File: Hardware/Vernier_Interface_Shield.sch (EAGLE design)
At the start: 43 parts, among them U1 74HC4052SO, U2 LMV358SOICT

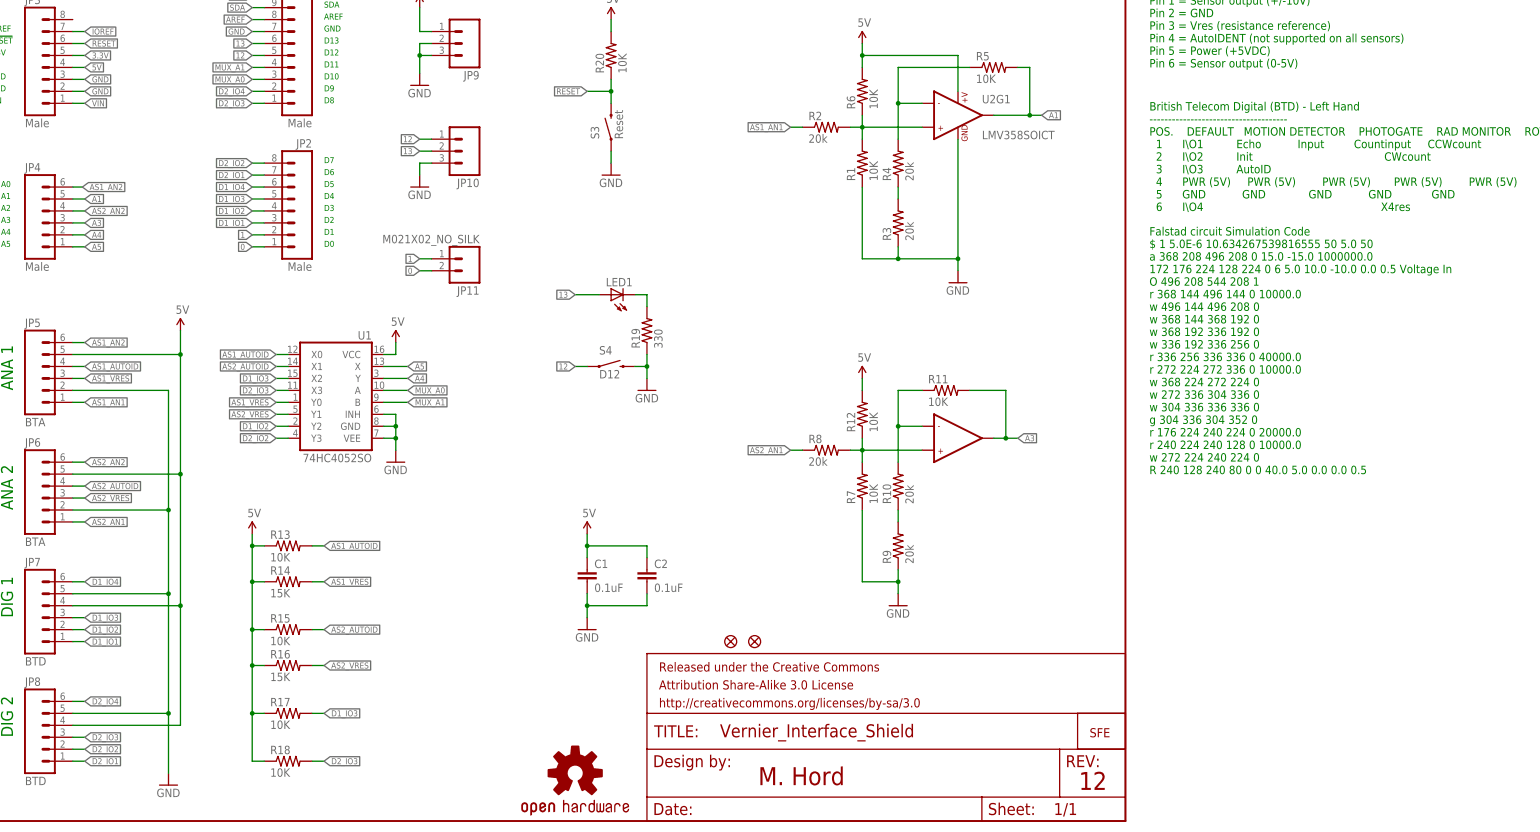
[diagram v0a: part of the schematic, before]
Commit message: Changed silk to fix bug #4
Changed silk to start at IO0 instead of IO1. This is per Vernier's
request.
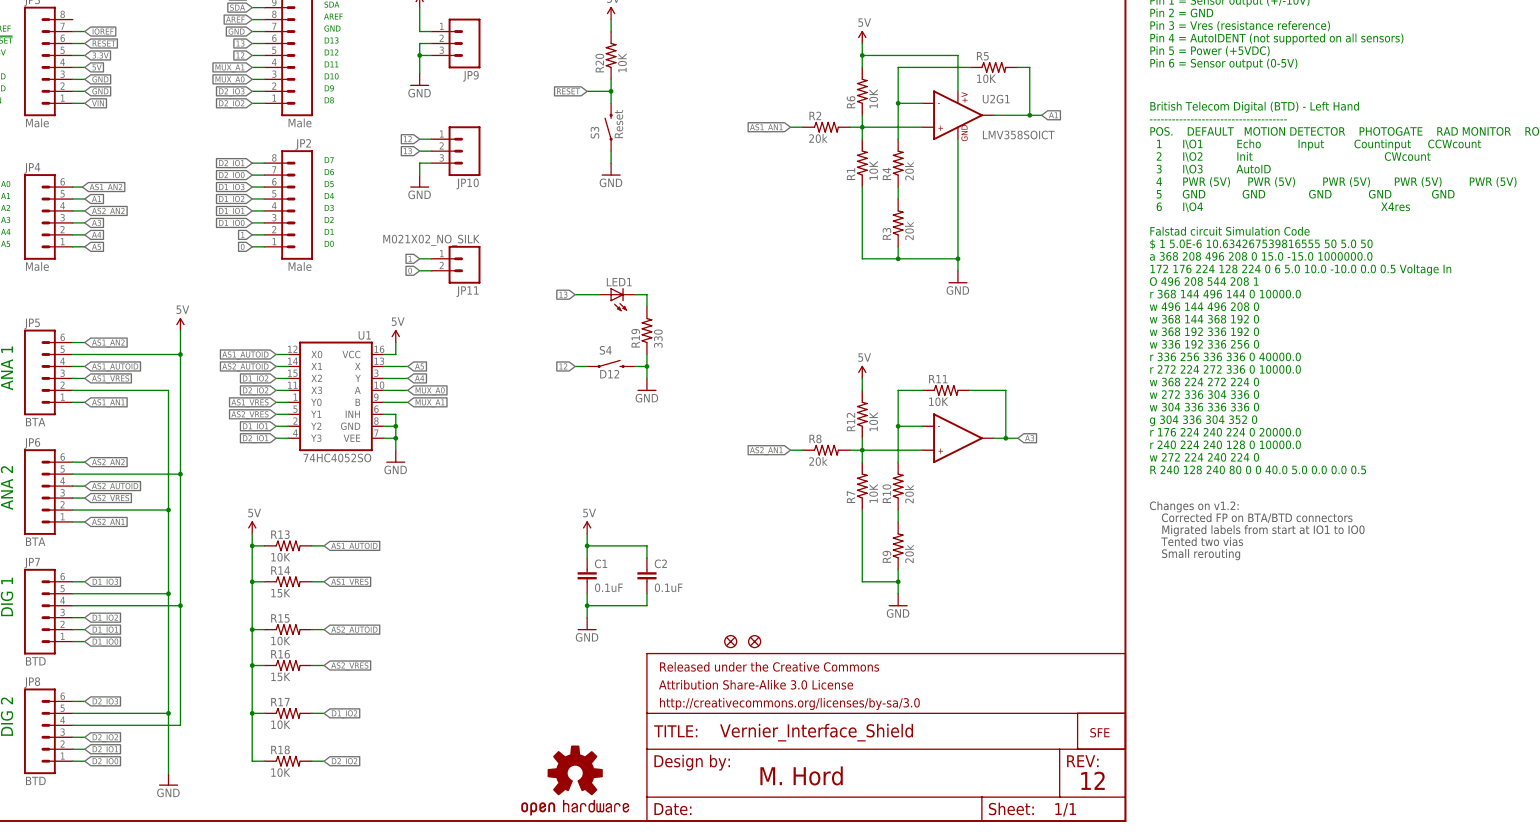
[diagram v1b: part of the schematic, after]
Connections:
- removed net D1_IO4: JP2.6, JP7.6
- removed net D2_IO4: JP1.2, JP8.6
- new net D1_IO0: JP2.3, JP7.1
- new net D2_IO0: JP2.7, JP8.1
- net D1_IO1: now also JP2.4, JP7.2, U1.Y2; no longer JP2.3, JP7.1
- net D1_IO2: now also JP2.5, JP7.3, R17.2, U1.X2; no longer JP2.4, JP7.2, U1.Y2
- net D1_IO3: now also JP2.6, JP7.6; no longer JP2.5, JP7.3, R17.2, U1.X2
- net D2_IO1: now also JP2.8, JP8.2, U1.Y3; no longer JP2.7, JP8.1
- net D2_IO2: now also JP1.1, JP8.3, R18.2, U1.X3; no longer JP2.8, JP8.2, U1.Y3
- net D2_IO3: now also JP1.2, JP8.6; no longer JP1.1, JP8.3, R18.2, U1.X3
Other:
- note added: "Changes on v1.2:"
- note added: "Corrected FP on BTA/BTD connectors"
- note added: "Migrated labels from start at IO1 to IO0"
- note added: "Small rerouting"
- note added: "Tented two vias"
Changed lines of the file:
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@@
 w 272 224 240 224 0
 R 240 128 240 80 0 0 40.0 5.0 0.0 0.0 0.5</text>
+<text x="254" y="66.04" size="1.778" layer="97">Changes on v1.2:</text>
+<text x="256.54" y="63.5" size="1.778" layer="97">Corrected FP on BTA/BTD connectors</text>
+<text x="256.54" y="60.96" size="1.778" layer="97">Migrated labels from start at IO1 to IO0</text>
+<text x="256.54" y="58.42" size="1.778" layer="97">Tented two vias</text>
+<text x="256.54" y="55.88" size="1.778" layer="97">Small rerouting</text>
 </plain>
 <instances>
@@
 </segment>
 </net>
-<net name="D2_IO4" class="0">
+<net name="D2_IO3" class="0">
 <segment>
 <wire x1="25.4" y1="25.4" x2="27.94" y2="25.4" width="0.1524" layer="91"/>
@@
 </segment>
 </net>
-<net name="D2_IO3" class="0">
+<net name="D2_IO2" class="0">
 <segment>
 <wire x1="25.4" y1="17.78" x2="27.94" y2="17.78" width="0.1524" layer="91"/>
@@
 </segment>
 </net>
-<net name="D2_IO2" class="0">
+<net name="D2_IO1" class="0">
 <segment>
 <wire x1="25.4" y1="15.24" x2="27.94" y2="15.24" width="0.1524" layer="91"/>
@@
 </segment>
 </net>
-<net name="D2_IO1" class="0">
+<net name="D2_IO0" class="0">
 <segment>
 <wire x1="25.4" y1="12.7" x2="27.94" y2="12.7" width="0.1524" layer="91"/>
@@
 </segment>
 </net>
-<net name="D1_IO4" class="0">
+<net name="D1_IO3" class="0">
 <segment>
 <wire x1="25.4" y1="50.8" x2="27.94" y2="50.8" width="0.1524" layer="91"/>
@@
 </segment>
 </net>
-<net name="D1_IO3" class="0">
+<net name="D1_IO2" class="0">
 <segment>
 <wire x1="25.4" y1="43.18" x2="27.94" y2="43.18" width="0.1524" layer="91"/>
@@
 </segment>
 </net>
-<net name="D1_IO2" class="0">
+<net name="D1_IO1" class="0">
 <segment>
 <wire x1="25.4" y1="40.64" x2="27.94" y2="40.64" width="0.1524" layer="91"/>
@@
 </segment>
 </net>
-<net name="D1_IO1" class="0">
+<net name="D1_IO0" class="0">
 <segment>
 <wire x1="27.94" y1="38.1" x2="25.4" y2="38.1" width="0.1524" layer="91"/>

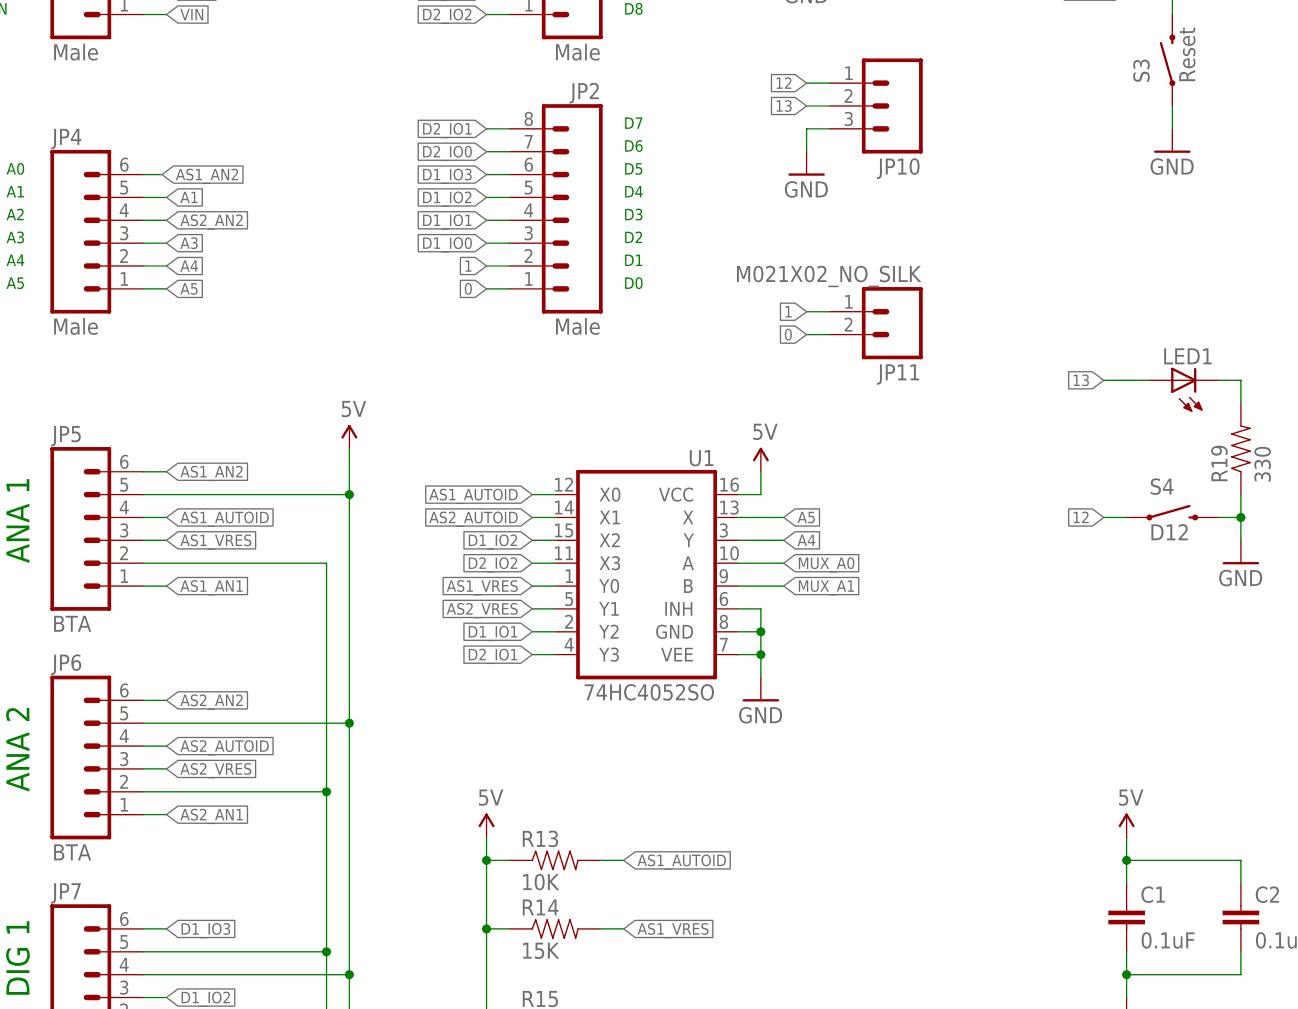
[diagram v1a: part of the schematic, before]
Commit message: Updated A0-A5 vias to be exposed to allow for probe pins
Swapped out 6 vias on A0 to A5 with M06 for exposed copper vias to allow
for probe points
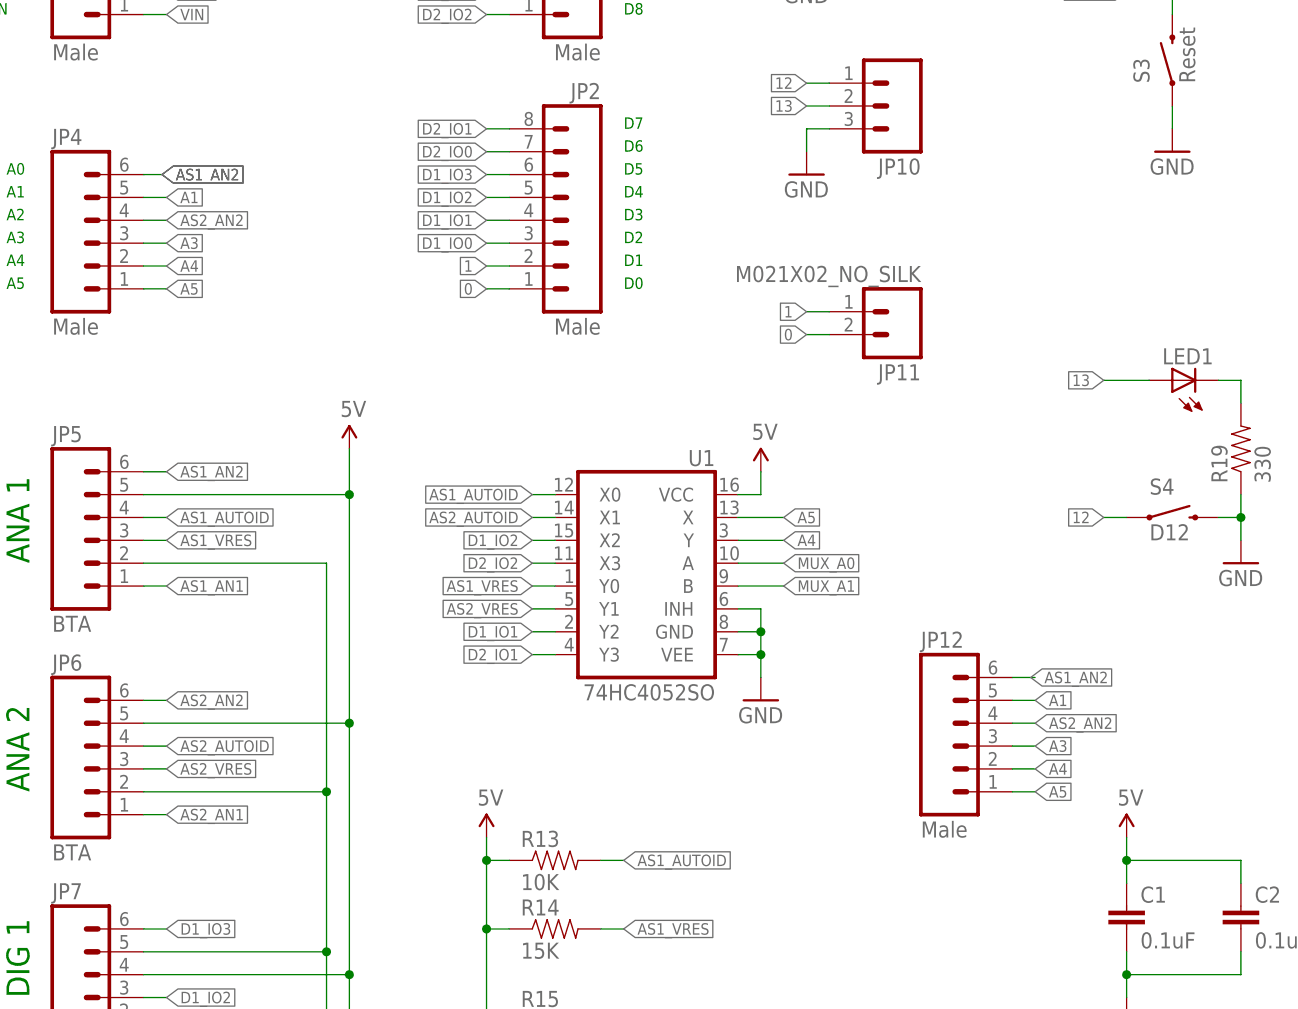
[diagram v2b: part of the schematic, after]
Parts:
- added JP12: Male, SparkFun-Connectors:M06SIP
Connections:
- net A1: now also JP12.5
- net A3: now also JP12.3
- net A4: now also JP12.2
- net A5: now also JP12.1
- net AS1_AN2: now also JP12.6
- net AS2_AN2: now also JP12.4
